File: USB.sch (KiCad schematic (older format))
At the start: 10 parts, among them J2 USB_C_Receptacle, U2 CH340C

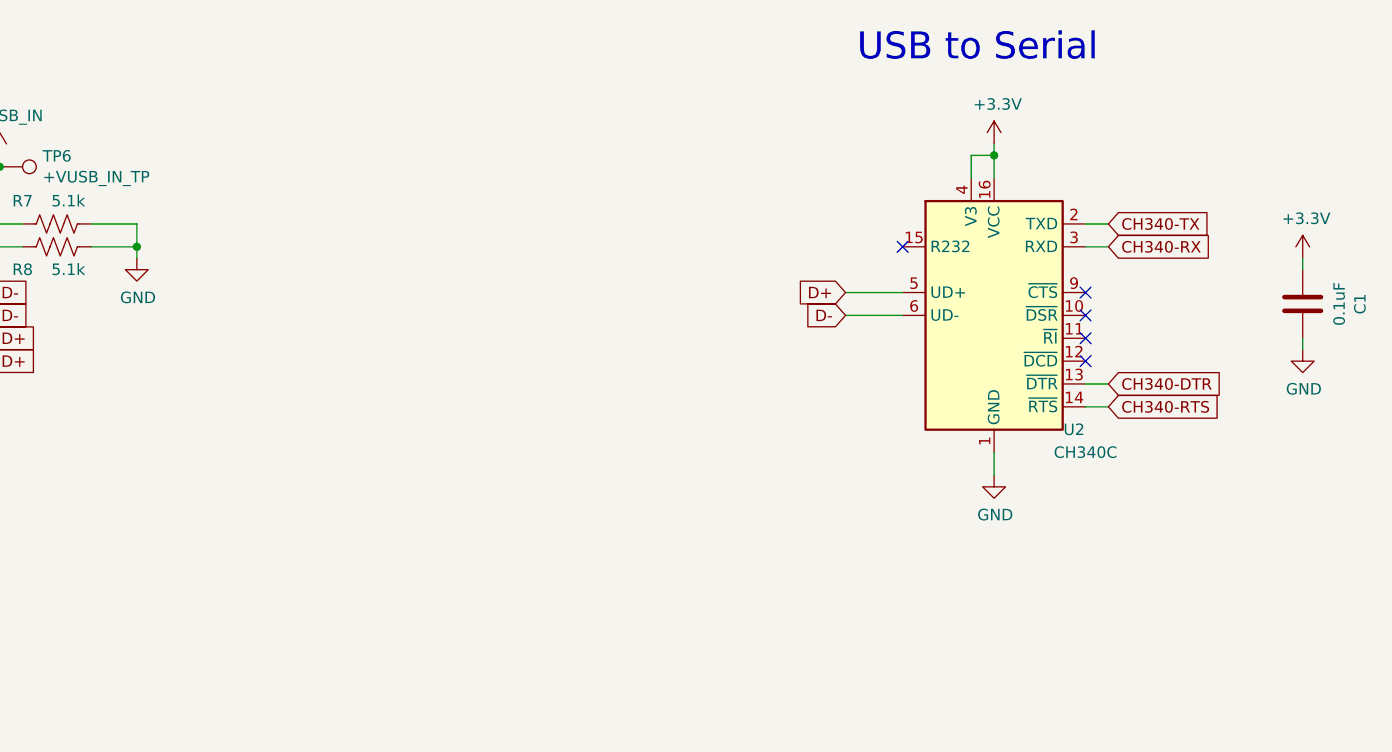
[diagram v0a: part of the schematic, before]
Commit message: Replace USB to UART with CP2102-GM
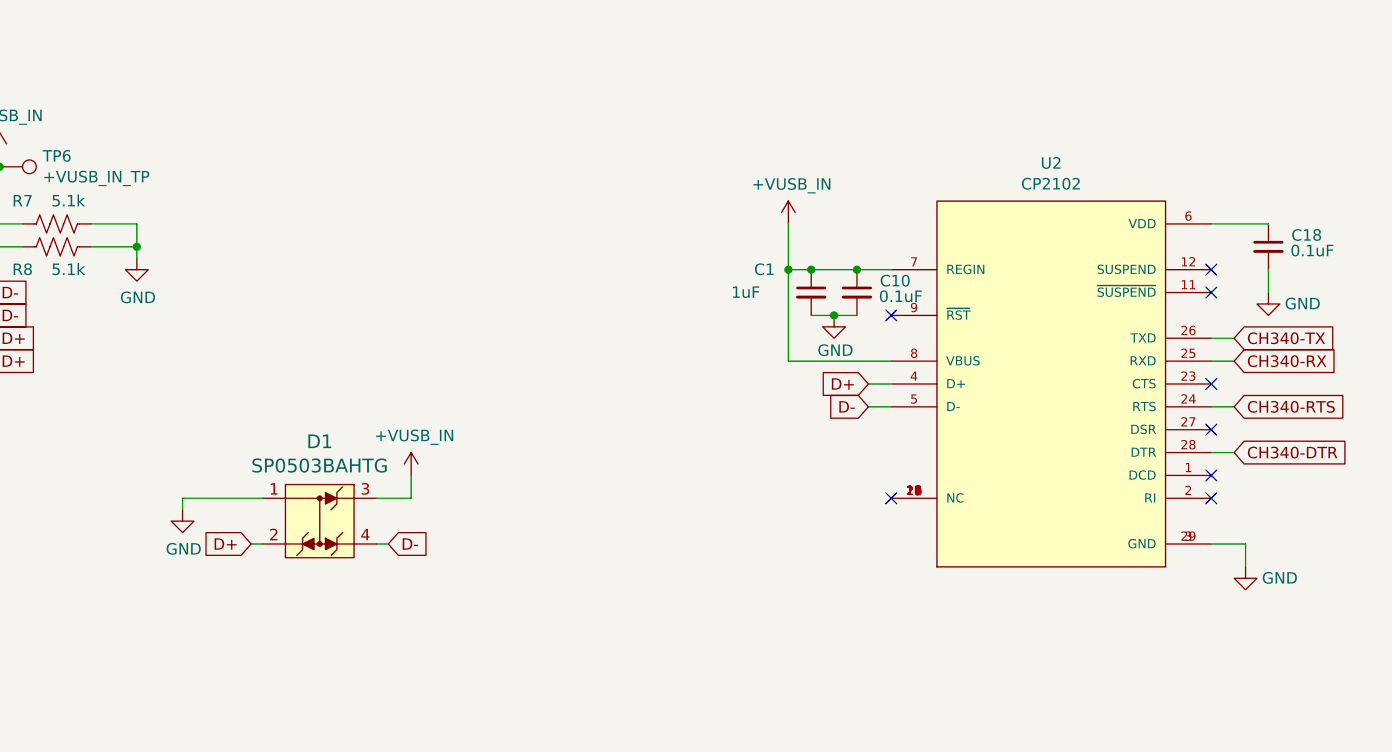
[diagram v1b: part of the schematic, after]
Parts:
- removed C1: 0.1uF, Capacitor_SMD:C_0603_1608Metric, symbol Device:C
- removed U2: CH340C, Package_SO:SOIC-16_3.9x9.9mm_P1.27mm, symbol Interface_USB:CH340C
- added C1: 1uF, symbol Device:C_Small
- added C10, C18: 0.1uF, Capacitor_SMD:C_0603_1608Metric, symbol Device:C_Small
- added D1: SP0503BAHTG, digikey-footprints:SOT-143-4, symbol dk_TVS-Diodes:SP0503BAHTG
- added U2: CP2102, CP2102:QFN50P500X500X100-29N, symbol CP2102:CP2102
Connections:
- net +VUSB_IN: now also C1.1, C10.1, D1.3, U2.7 (REGIN), U2.8 (VBUS)
- net CH340-DTR: now also U2.28 (DTR)
- net CH340-RTS: now also U2.24 (RTS)
- net CH340-RX: now also U2.25 (RXD)
- net CH340-TX: now also U2.26 (TXD)
- net D+: now also D1.2, U2.4 (D+)
- net D-: now also D1.4, U2.5 (D-)
- net GND: now also C1.2, C10.2, C18.2, D1.1, U2.29 (GND), U2.3 (GND)
- new net: U2.10 (NC), U2.13 (NC), U2.14 (NC), U2.15 (NC), U2.16 (NC), U2.17 (NC), U2.18 (NC), U2.19 (NC), U2.20 (NC), U2.21 (NC), U2.22 (NC)
- new net: C18.1, U2.6 (VDD)
- no-connect marks 16 -> 19
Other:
- note removed: "USB to Serial"

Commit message: Update board
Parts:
- added C19: 4.7uF, Capacitor_SMD:C_0805_2012Metric, symbol Device:C_Small
- C1: footprint (none) -> Capacitor_SMD:C_0603_1608Metric; DigiKey (none) -> https://www.digikey.com/en/products/detail/kemet/C0603C105K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
- C10, C18: DigiKey (none) -> https://www.digikey.com/en/products/detail/kemet/C0603C104J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
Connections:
- net +VUSB_IN: no longer C1.1, C10.1, U2.7 (REGIN)
- net GND: now also C19.2
- net +3V3: now reaches C18.1, U2.6 (VDD)
- net +3V3: now also C1.1, C10.1, U2.7 (REGIN), C19.1
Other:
- moved on the sheet: C1, C10, C18, D1, J2, R7, R8, TP6, U2
